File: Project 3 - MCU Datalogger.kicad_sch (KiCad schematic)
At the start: 25 parts, among them U1 24LC1025, U2 24LC1025, U3 ATMEGA328P-AU, U4 DS1337S+, Y1 Crystal, Y2 Crystal

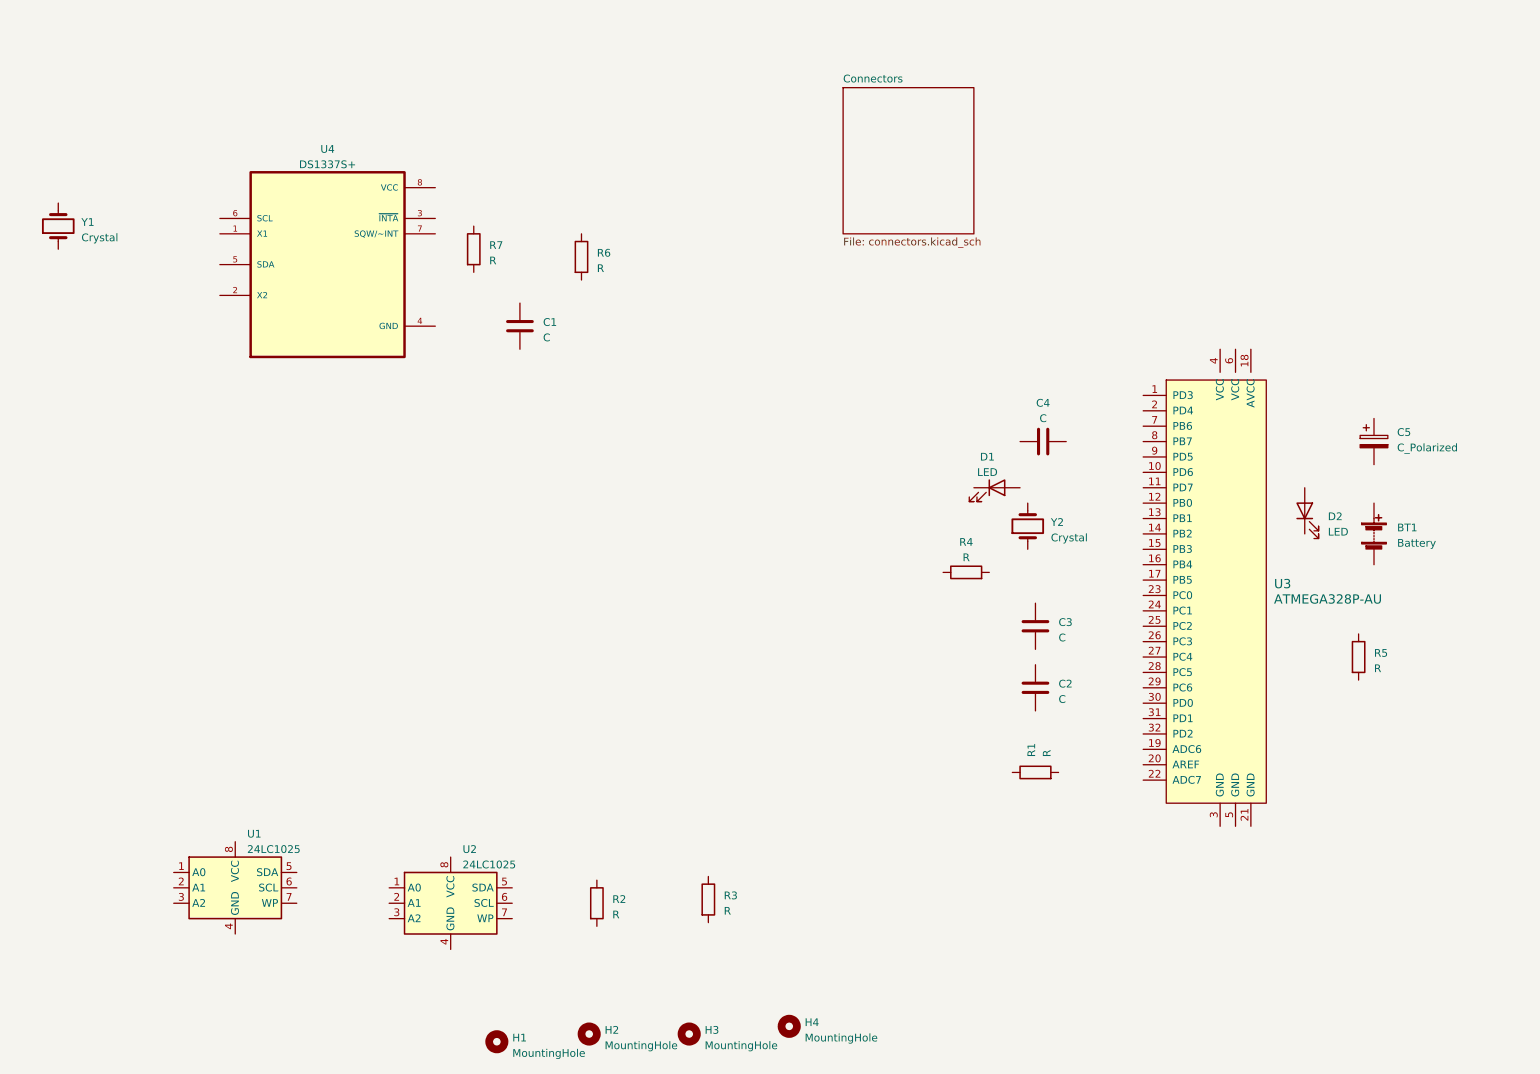
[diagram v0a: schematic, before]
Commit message: added component values in schema
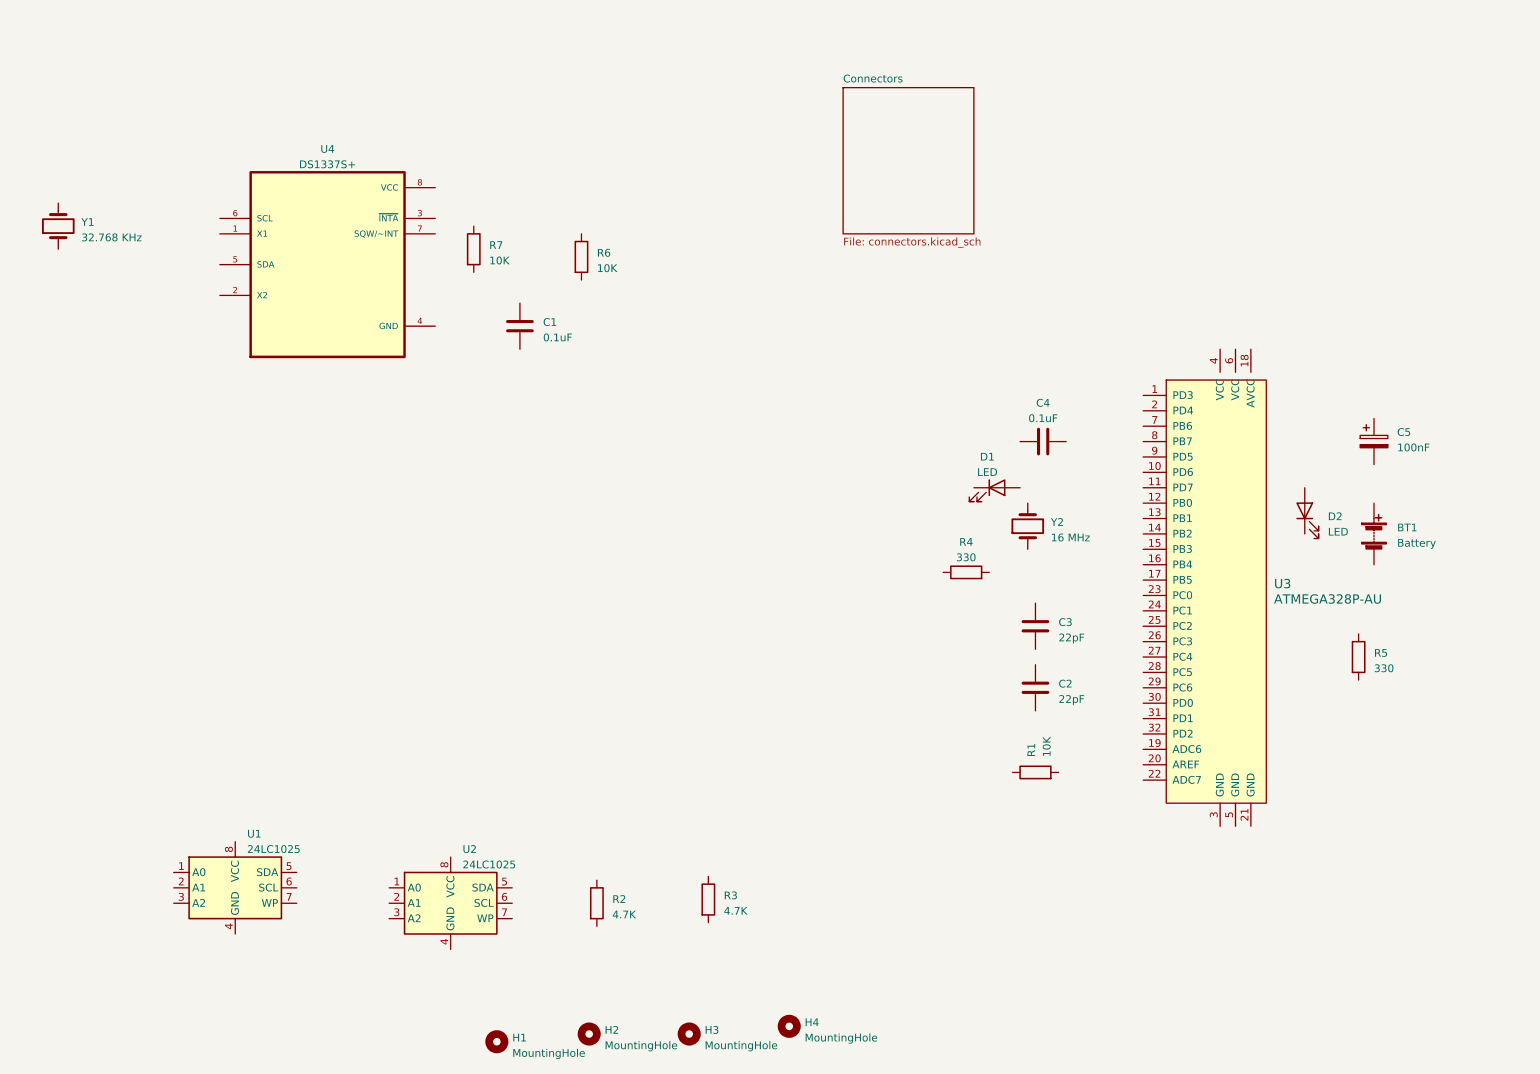
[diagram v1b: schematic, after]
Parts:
- C1, C4: value C -> 0.1uF
- C2, C3: value C -> 22pF
- C5: value C_Polarized -> 100nF
- R1, R6, R7: value R -> 10K
- R2, R3: value R -> 4.7K
- R4, R5: value R -> 330
- Y1: value Crystal -> 32.768 KHz
- Y2: value Crystal -> 16 MHz
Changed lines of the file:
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@@
       (effects (font (size 1.27 1.27)) (justify left))
     )
-    (property "Value" "R" (at 203.835 139.7 0)
+    (property "Value" "10K" (at 203.835 139.7 0)
       (effects (font (size 1.27 1.27)) (justify left))
     )
@@
       (effects (font (size 1.27 1.27)) hide)
     )
+    (property "Purpose" "" (at 201.93 142.24 0)
+      (effects (font (size 1.27 1.27)))
+    )
     (pin "1")
     (pin "2")
@@
       (effects (font (size 1.27 1.27)) (justify left))
     )
-    (property "Value" "R" (at 111.76 57.785 0)
+    (property "Value" "10K" (at 111.76 57.785 0)
       (effects (font (size 1.27 1.27)) (justify left))
     )
@@
     (property "Datasheet" "~" (at 109.22 55.88 0)
       (effects (font (size 1.27 1.27)) hide)
+    )
+    (property "Purpose" "" (at 109.22 55.88 0)
+      (effects (font (size 1.27 1.27)))
     )
     (pin "1")
@@
       (effects (font (size 1.27 1.27)) (justify right))
     )
-    (property "Value" "Crystal" (at 44.45 53.975 90)
+    (property "Value" "32.768 KHz" (at 44.45 53.975 90)
       (effects (font (size 1.27 1.27)) (justify right))
     )
@@
     (property "Datasheet" "~" (at 40.64 52.07 0)
       (effects (font (size 1.27 1.27)) hide)
+    )
+    (property "Purpose" "" (at 40.64 52.07 0)
+      (effects (font (size 1.27 1.27)))
     )
     (pin "1")
@@
       (effects (font (size 1.27 1.27)))
     )
-    (property "Value" "R" (at 190.5 106.7784 90)
+    (property "Value" "330" (at 190.5 106.7784 90)
       (effects (font (size 1.27 1.27)))
     )
@@
       (effects (font (size 1.27 1.27)) hide)
     )
+    (property "Purpose" "" (at 190.5 109.22 0)
+      (effects (font (size 1.27 1.27)))
+    )
     (pin "1")
     (pin "2")
@@
       (effects (font (size 1.27 1.27)) (justify left))
     )
-    (property "Value" "R" (at 132.08 165.735 0)
+    (property "Value" "4.7K" (at 132.08 165.735 0)
       (effects (font (size 1.27 1.27)) (justify left))
     )
@@
       (effects (font (size 1.27 1.27)) hide)
     )
+    (property "Purpose" "" (at 129.54 163.83 0)
+      (effects (font (size 1.27 1.27)))
+    )
     (pin "1")
     (pin "2")
@@
       (effects (font (size 1.27 1.27)) (justify left))
     )
-    (property "Value" "R" (at 257.81 125.095 0)
+    (property "Value" "330" (at 257.81 125.095 0)
       (effects (font (size 1.27 1.27)) (justify left))
     )
@@
     (property "Datasheet" "~" (at 255.27 123.19 0)
       (effects (font (size 1.27 1.27)) hide)
+    )
+    (property "Purpose" "" (at 255.27 123.19 0)
+      (effects (font (size 1.27 1.27)))
     )
     (pin "1")
@@
       (effects (font (size 1.27 1.27)) (justify right))
     )
-    (property "Value" "Crystal" (at 204.47 103.505 90)
+    (property "Value" "16 MHz" (at 204.47 103.505 90)
       (effects (font (size 1.27 1.27)) (justify right))
     )
@@
       (effects (font (size 1.27 1.27)) hide)
     )
+    (property "Purpose" "" (at 200.66 101.6 0)
+      (effects (font (size 1.27 1.27)))
+    )
     (pin "1")
     (pin "2")
@@
       (effects (font (size 1.27 1.27)))
     )
-    (property "Value" "C" (at 203.2 83.82 90)
+    (property "Value" "0.1uF" (at 203.2 83.82 90)
       (effects (font (size 1.27 1.27)))
     )
@@
     (property "Datasheet" "~" (at 203.2 87.63 0)
       (effects (font (size 1.27 1.27)) hide)
+    )
+    (property "Purpose" "" (at 203.2 87.63 0)
+      (effects (font (size 1.27 1.27)))
     )
     (pin "1")
@@
       (effects (font (size 1.27 1.27)) (justify left))
     )
-    (property "Value" "C" (at 205.74 120.015 0)
+    (property "Value" "22pF" (at 205.74 120.015 0)
       (effects (font (size 1.27 1.27)) (justify left))
     )
@@
       (effects (font (size 1.27 1.27)) hide)
     )
+    (property "Purpose" "" (at 201.93 118.11 0)
+      (effects (font (size 1.27 1.27)))
+    )
     (pin "1")
     (pin "2")
@@
       (effects (font (size 1.27 1.27)) (justify left))
     )
-    (property "Value" "C_Polarized" (at 261.62 88.646 0)
+    (property "Value" "100nF" (at 261.62 88.646 0)
       (effects (font (size 1.27 1.27)) (justify left))
     )
@@
       (effects (font (size 1.27 1.27)) hide)
     )
+    (property "Purpose" "" (at 257.81 87.63 0)
+      (effects (font (size 1.27 1.27)))
+    )
     (pin "1")
     (pin "2")
@@
       (effects (font (size 1.27 1.27)) (justify left))
     )
-    (property "Value" "C" (at 205.74 130.175 0)
+    (property "Value" "22pF" (at 205.74 130.175 0)
       (effects (font (size 1.27 1.27)) (justify left))
     )
@@
       (effects (font (size 1.27 1.27)) hide)
     )
+    (property "Purpose" "" (at 201.93 128.27 0)
+      (effects (font (size 1.27 1.27)))
+    )
     (pin "1")
     (pin "2")
@@
       (effects (font (size 1.27 1.27)) (justify left))
     )
-    (property "Value" "C" (at 120.65 70.485 0)
+    (property "Value" "0.1uF" (at 120.65 70.485 0)
       (effects (font (size 1.27 1.27)) (justify left))
     )
@@
     (property "Datasheet" "~" (at 116.84 68.58 0)
       (effects (font (size 1.27 1.27)) hide)
+    )
+    (property "Purpose" "" (at 116.84 68.58 0)
+      (effects (font (size 1.27 1.27)))
     )
     (pin "1")
@@
       (effects (font (size 1.27 1.27)) (justify left))
     )
-    (property "Value" "R" (at 129.54 59.055 0)
+    (property "Value" "10K" (at 129.54 59.055 0)
       (effects (font (size 1.27 1.27)) (justify left))
     )
@@
       (effects (font (size 1.27 1.27)) hide)
     )
+    (property "Purpose" "" (at 127 57.15 0)
+      (effects (font (size 1.27 1.27)))
+    )
     (pin "1")
     (pin "2")
@@
       (effects (font (size 1.27 1.27)) (justify left))
     )
-    (property "Value" "R" (at 150.4796 165.1251 0)
+    (property "Value" "4.7K" (at 150.4796 165.1251 0)
       (effects (font (size 1.27 1.27)) (justify left))
     )
@@
       (effects (font (size 1.27 1.27)) hide)
     )
-    (pin "1")
+    (property "Purpose" "" (at 147.9396 163.2201 0)
+      (effects (font (size 1.27 1.27)))
+    )
+    (pin "1")

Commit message: Assigned footprints to symbols
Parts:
- BT1: footprint (none) -> Connector_PinHeader_2.54mm:PinHeader_1x02_P2.54mm_Vertical
- C1, C2, C3, C4, C5: footprint (none) -> Capacitor_SMD:C_0805_2012Metric
- D1, D2: footprint (none) -> LED_SMD:LED_0805_2012Metric
- H1, H2, H3, H4: footprint (none) -> MountingHole:MountingHole_2.1mm
- R1, R2, R3, R4, R5, R6, R7: footprint (none) -> Resistor_SMD:R_0805_2012Metric
- U1, U2: footprint (none) -> Package_SO:SOIC-8_5.23x5.23mm_P1.27mm
- U3: footprint digikey-footprints:TQFP-32_7x7mm -> Datalogger Clock Footprints:QFP80P900X900X120-32N
- U4: footprint SOIC127P600X175-8N -> Datalogger Clock Footprints:SOIC127P600X175-8N
- Y1, Y2: footprint (none) -> Crystal:Crystal_SMD_5032-2Pin_5.0x3.2mm_HandSoldering
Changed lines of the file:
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@@
       (effects (font (size 1.524 1.524)) (justify left))
     )
-    (property "Footprint" "digikey-footprints:TQFP-32_7x7mm" (at 237.49 107.95 0)
+    (property "Footprint" "Datalogger Clock Footprints:QFP80P900X900X120-32N" (at 237.49 107.95 0)
       (effects (font (size 1.524 1.524)) (justify left) hide)
     )
@@
       (effects (font (size 1.27 1.27)) (justify left))
     )
-    (property "Footprint" "" (at 201.93 144.018 90)
+    (property "Footprint" "Resistor_SMD:R_0805_2012Metric" (at 201.93 144.018 90)
       (effects (font (size 1.27 1.27)) hide)
     )
@@
       (effects (font (size 1.27 1.27)) (justify left))
     )
-    (property "Footprint" "" (at 144.78 185.42 0)
+    (property "Footprint" "MountingHole:MountingHole_2.1mm" (at 144.78 185.42 0)
       (effects (font (size 1.27 1.27)) hide)
     )
@@
       (effects (font (size 1.27 1.27)) (justify left))
     )
-    (property "Footprint" "" (at 107.442 55.88 90)
+    (property "Footprint" "Resistor_SMD:R_0805_2012Metric" (at 107.442 55.88 90)
       (effects (font (size 1.27 1.27)) hide)
     )
@@
       (effects (font (size 1.27 1.27)) (justify left))
     )
-    (property "Footprint" "" (at 128.27 185.42 0)
+    (property "Footprint" "MountingHole:MountingHole_2.1mm" (at 128.27 185.42 0)
       (effects (font (size 1.27 1.27)) hide)
     )
@@
       (effects (font (size 1.27 1.27)) (justify right))
     )
-    (property "Footprint" "" (at 40.64 52.07 0)
+    (property "Footprint" "Crystal:Crystal_SMD_5032-2Pin_5.0x3.2mm_HandSoldering" (at 40.64 52.07 0)
       (effects (font (size 1.27 1.27)) hide)
     )
@@
       (effects (font (size 1.27 1.27)) (justify left))
     )
-    (property "Footprint" "" (at 161.29 184.15 0)
+    (property "Footprint" "MountingHole:MountingHole_2.1mm" (at 161.29 184.15 0)
       (effects (font (size 1.27 1.27)) hide)
     )
@@
       (effects (font (size 1.27 1.27)))
     )
-    (property "Footprint" "SOIC127P600X175-8N" (at 85.09 58.42 0)
+    (property "Footprint" "Datalogger Clock Footprints:SOIC127P600X175-8N" (at 85.09 58.42 0)
       (effects (font (size 1.27 1.27)) (justify bottom) hide)
     )
@@
       (effects (font (size 1.27 1.27)))
     )
-    (property "Footprint" "" (at 190.5 110.998 90)
+    (property "Footprint" "Resistor_SMD:R_0805_2012Metric" (at 190.5 110.998 90)
       (effects (font (size 1.27 1.27)) hide)
     )
@@
       (effects (font (size 1.27 1.27)) (justify left))
     )
-    (property "Footprint" "" (at 127.762 163.83 90)
+    (property "Footprint" "Resistor_SMD:R_0805_2012Metric" (at 127.762 163.83 90)
       (effects (font (size 1.27 1.27)) hide)
     )
@@
       (effects (font (size 1.27 1.27)) (justify left))
     )
-    (property "Footprint" "" (at 253.492 123.19 90)
+    (property "Footprint" "Resistor_SMD:R_0805_2012Metric" (at 253.492 123.19 90)
       (effects (font (size 1.27 1.27)) hide)
     )
@@
       (effects (font (size 1.27 1.27)) (justify right))
     )
-    (property "Footprint" "" (at 200.66 101.6 0)
+    (property "Footprint" "Crystal:Crystal_SMD_5032-2Pin_5.0x3.2mm_HandSoldering" (at 200.66 101.6 0)
       (effects (font (size 1.27 1.27)) hide)
     )
@@
       (effects (font (size 1.27 1.27)))
     )
-    (property "Footprint" "" (at 207.01 86.6648 0)
+    (property "Footprint" "Capacitor_SMD:C_0805_2012Metric" (at 207.01 86.6648 0)
       (effects (font (size 1.27 1.27)) hide)
     )
@@
       (effects (font (size 1.27 1.27)) (justify left))
     )
-    (property "Footprint" "" (at 105.41 163.83 0)
+    (property "Footprint" "Package_SO:SOIC-8_5.23x5.23mm_P1.27mm" (at 105.41 163.83 0)
       (effects (font (size 1.27 1.27)) hide)
     )
@@
       (effects (font (size 1.27 1.27)) (justify left))
     )
-    (property "Footprint" "" (at 202.8952 121.92 0)
+    (property "Footprint" "Capacitor_SMD:C_0805_2012Metric" (at 202.8952 121.92 0)
       (effects (font (size 1.27 1.27)) hide)
     )
@@
       (effects (font (size 1.27 1.27)) (justify left))
     )
-    (property "Footprint" "" (at 258.7752 91.44 0)
+    (property "Footprint" "Capacitor_SMD:C_0805_2012Metric" (at 258.7752 91.44 0)
       (effects (font (size 1.27 1.27)) hide)
     )
@@
       (effects (font (size 1.27 1.27)) (justify left))
     )
-    (property "Footprint" "" (at 113.03 186.69 0)
+    (property "Footprint" "MountingHole:MountingHole_2.1mm" (at 113.03 186.69 0)
       (effects (font (size 1.27 1.27)) hide)
     )
@@
       (effects (font (size 1.27 1.27)) (justify left))
     )
-    (property "Footprint" "" (at 202.8952 132.08 0)
+    (property "Footprint" "Capacitor_SMD:C_0805_2012Metric" (at 202.8952 132.08 0)
       (effects (font (size 1.27 1.27)) hide)
     )
@@
       (effects (font (size 1.27 1.27)) (justify left))
     )
-    (property "Footprint" "" (at 117.8052 72.39 0)
+    (property "Footprint" "Capacitor_SMD:C_0805_2012Metric" (at 117.8052 72.39 0)
       (effects (font (size 1.27 1.27)) hide)
     )
@@
       (effects (font (size 1.27 1.27)))
     )
-    (property "Footprint" "" (at 195.58 95.25 0)
+    (property "Footprint" "LED_SMD:LED_0805_2012Metric" (at 195.58 95.25 0)
       (effects (font (size 1.27 1.27)) hide)
     )
@@
       (effects (font (size 1.27 1.27)) (justify right))
     )
-    (property "Footprint" "" (at 246.38 99.06 0)
+    (property "Footprint" "LED_SMD:LED_0805_2012Metric" (at 246.38 99.06 0)
       (effects (font (size 1.27 1.27)) hide)
     )
@@
       (effects (font (size 1.27 1.27)) (justify left))
     )
-    (property "Footprint" "" (at 69.85 161.29 0)
+    (property "Footprint" "Package_SO:SOIC-8_5.23x5.23mm_P1.27mm" (at 69.85 161.29 0)
       (effects (font (size 1.27 1.27)) hide)
     )
@@
       (effects (font (size 1.27 1.27)) (justify left))
     )
-    (property "Footprint" "" (at 125.222 57.15 90)
+    (property "Footprint" "Resistor_SMD:R_0805_2012Metric" (at 125.222 57.15 90)
       (effects (font (size 1.27 1.27)) hide)
     )
@@
       (effects (font (size 1.27 1.27)) (justify left))
     )
-    (property "Footprint" "" (at 146.1616 163.2201 90)
+    (property "Footprint" "Resistor_SMD:R_0805_2012Metric" (at 146.1616 163.2201 90)
       (effects (font (size 1.27 1.27)) hide)
     )
@@
       (effects (font (size 1.27 1.27)) (justify left))
     )
-    (property "Footprint" "" (at 257.81 101.346 90)
-      (effects (font (size 1.27 1.27)) hide)
-    )
+    (property "Footprint" "Connector_PinHeader_2.54mm:PinHeader_1x02_P2.54mm_Vertical" (at 257.81 101.346 90)
+      (effects (font (size 1.27 1.27)) hide)
+    )

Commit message: completed writing in schematic sheet 1
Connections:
- net at U3.17 (PB5): now also D1.2 (A)
- net at U3.18 (AVCC): now also BT1.1 (+), C5.1, D2.2 (A)
- net at U3.20 (AREF): now also C4.2
- net GND: now reaches U3.21 (GND)
- net GND: now also BT1.2 (-), C1.2, C2.1, C3.1, C4.1, C5.2, R4.1, R5.2, U1.4 (GND), U1.7 (WP), U2.2 (A1), U2.4 (GND), U2.7 (WP), U3.3 (GND), U3.5 (GND), U4.4 (GND)
- net at U3.29 (PC6): now also R1.2
- net at U3.7 (PB6): now also C2.2, C3.2, Y2.1, Y2.2
- net Vcc: now reaches R1.1
- net Vcc: now also R2.1, R3.1, U1.1 (A0), U1.2 (A1), U1.3 (A2), U1.8 (VCC), U2.1 (A0), U2.3 (A2), U2.8 (VCC)
- net at R7.1: now also C1.1, R6.1, U4.8 (VCC)
- net at R7.2: now also U4.3 (~{INTA})
- net at Y1.1: now also U4.2 (X2)
- net at Y1.2: now also U4.1 (X1)
- net SDA: now reaches U4.5 (SDA)
- net SDA: now also R3.2, U1.5 (SDA), U2.5 (SDA)
- net SCK: now reaches U4.6 (SCL)
- net SCK: now also R2.2, U1.6 (SCL), U2.6 (SCL)
- net at U4.7 (SQW/~INT): now also R6.2
- net at R4.2: now also D1.1 (K)
- net at R5.1: now also D2.1 (K)
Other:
- moved on the sheet: BT1, C1, C2, C3, C4, C5, D1, D2, H1, H2, H3, H4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

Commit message: completed writing of embedded connector sheet
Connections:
- net SCK: now also D1.2 (A), U3.17 (PB5), U3.28 (PC5)
- net SDA: now also U3.27 (PC4)
- net D3: now reaches U3.1 (PD3)
- net D6: now reaches U3.10 (PD6)
- net D7: now reaches U3.11 (PD7)
- net D8: now reaches U3.12 (PB0)
- net MOSI: now reaches U3.15 (PB3)
- net MISO: now reaches U3.16 (PB4)
- net at BT1.1 (+), C5.1, D2.2 (A)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: now also U3.4 (VCC)
- net D4: now reaches U3.2 (PD4)
- net RESET: now reaches R1.2, U3.29 (PC6)
- net RX: now reaches U3.30 (PD0)
- net TX: now reaches U3.31 (PD1)
- net D2: now reaches U3.32 (PD2)
- net D5: now reaches U3.9 (PD5)
- no-connect marks 0 -> 10
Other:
- sheet Connectors ports: added D2, D3, D4, D5, D6, D7, D8, GND, MISO, MOSI, RESET, RX, SCK, SDA, TX, Vcc; removed none
